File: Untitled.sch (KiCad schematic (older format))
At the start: 14 parts

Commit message: rest of the electrical
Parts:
- added D1, D2, D3, D4: D_Small, Diode_SMD:D_SOD-123, symbol Device:D_Small
- added F1: Polyfuse_Small, Fuse:Fuse_1206_3216Metric, symbol Device:Polyfuse_Small
- added MX1, MX2, MX3, MX4: MX-NoLED, MX_Alps_Hybrid:MX-1.5U-NoLED, symbol MX_Alps_Hybrid:MX-NoLED
- added USB1: Molex-0548190589, random-keyboard-parts:Molex-0548190589, symbol random-keyboard-parts:Molex-0548190589
- C1, C2, C3, C4, C5, C6, C7: renamed from C?; footprint (none) -> Capacitor_SMD:C_0805_2012Metric
- R1, R2, R3, R4: renamed from R?; footprint (none) -> Resistor_SMD:R_0805_2012Metric
- SW1: renamed from SW?; footprint (none) -> random-keyboard-parts:SKQG-1155865
- Y1: renamed from Y?; footprint (none) -> Crystal:Crystal_SMD_3225-4Pin_3.2x2.5mm
- gave numbers to parts that had none: 1
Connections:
- net +5V: now also F1.1
- net D+: now also USB1.4 (D-)
- net D-: now also USB1.3 (D+)
- net GND: now also USB1.1 (GND)
- new net: D1.2 (A), MX1.2 (ROW)
- new net: D4.2 (A), MX4.2 (ROW)
- new net: D2.2 (A), MX2.2 (ROW)
- new net: D3.2 (A), MX3.2 (ROW)
- new net COL0: MX1.1 (COL), MX2.1 (COL)
- new net COL1: MX3.1 (COL), MX4.1 (COL)
- new net ROW0: D1.1 (K), D4.1 (K)
- new net ROW1: D2.1 (K), D3.1 (K)
- new net VCC: F1.2, USB1.5 (VBUS)

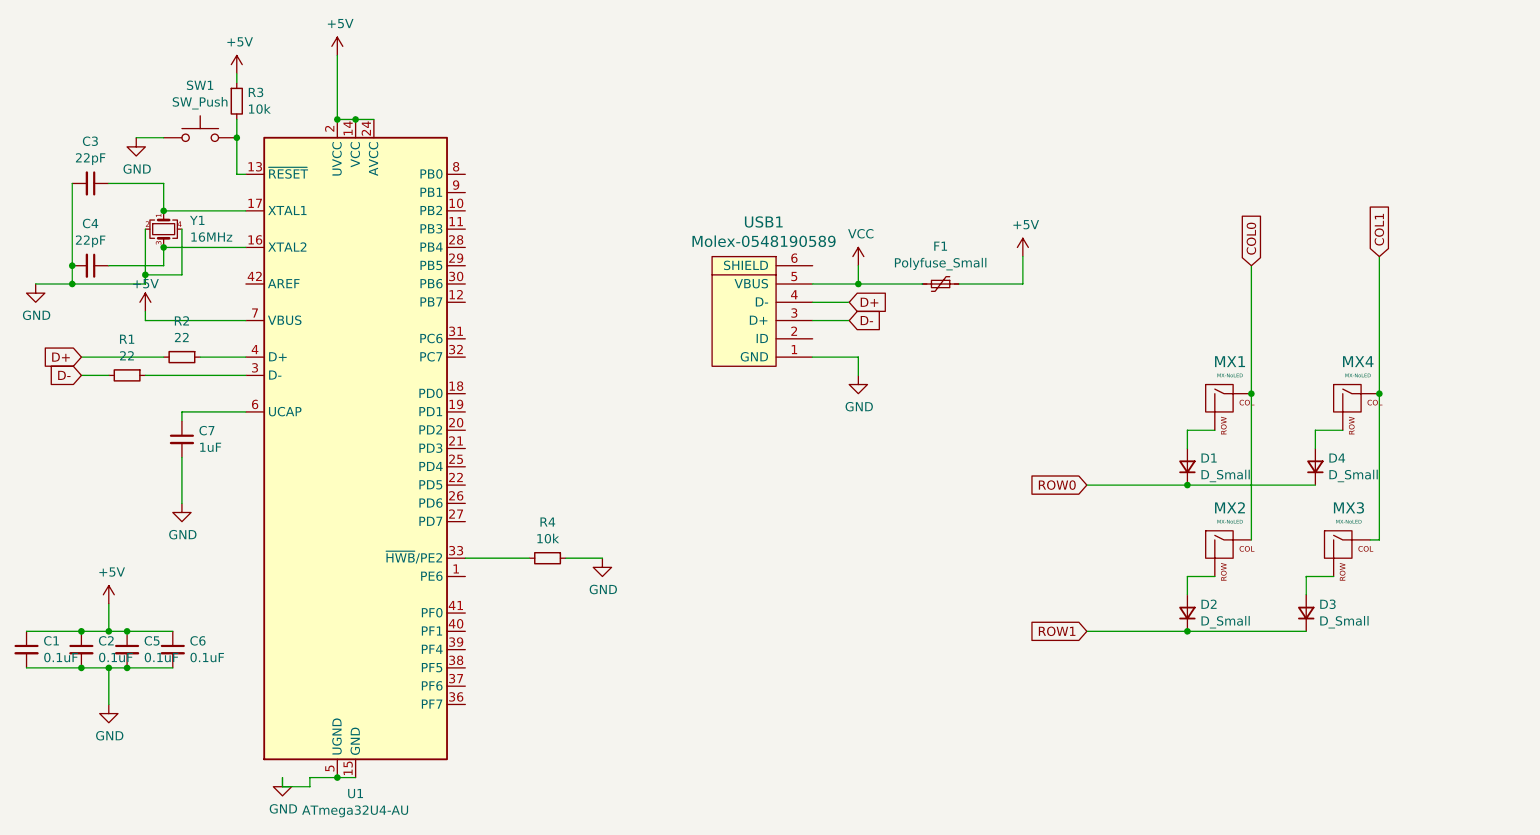
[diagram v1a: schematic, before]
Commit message: Routed MCU
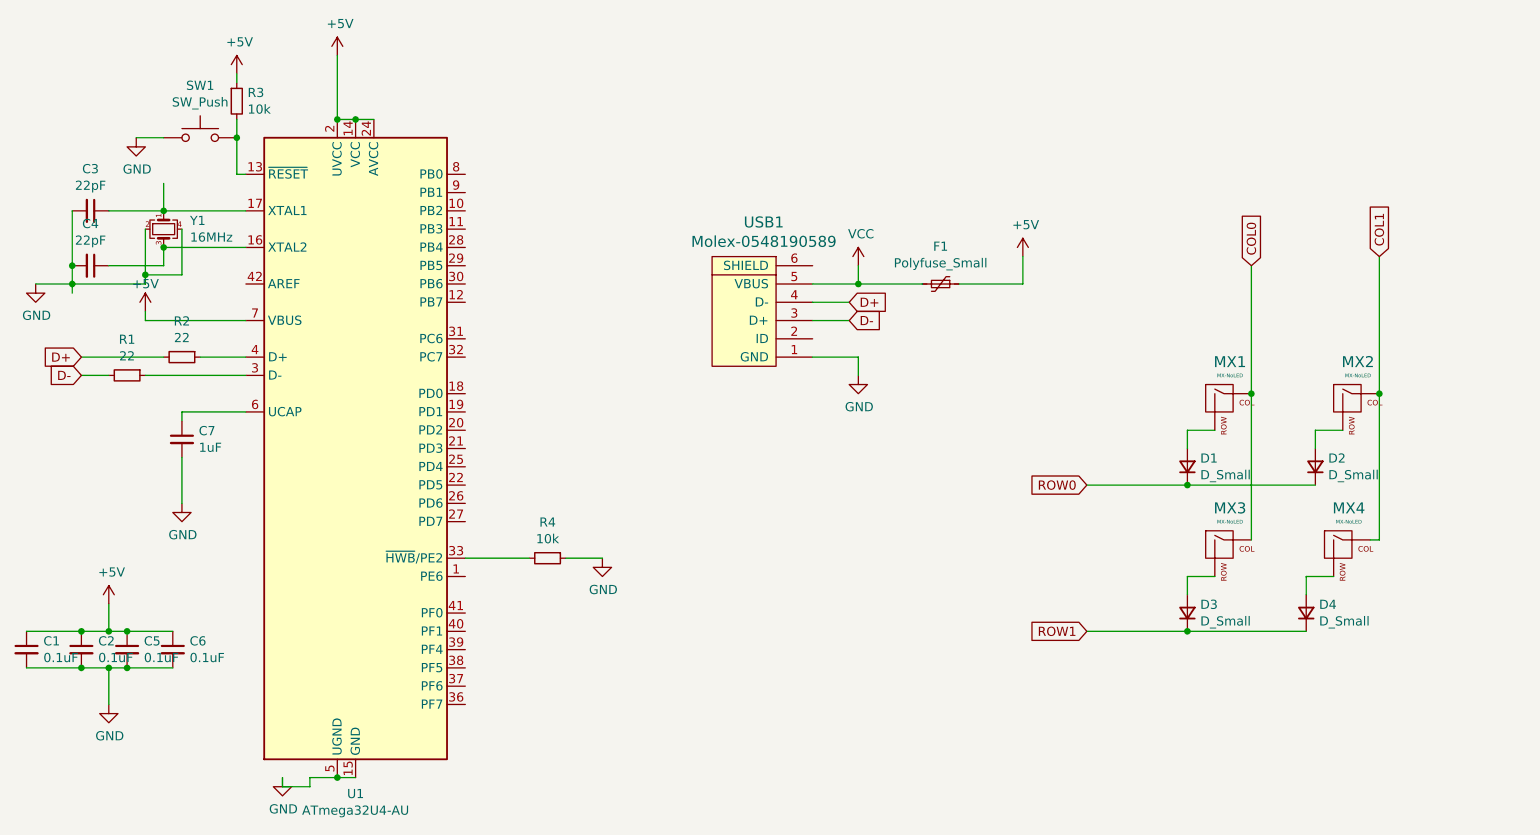
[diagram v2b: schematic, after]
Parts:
- renumbered D4 to D2, D2 to D3, D3 to D4, MX4 to MX2, MX2 to MX3, MX3 to MX4
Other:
- moved on the sheet: C3
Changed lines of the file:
@@
 L Device:C_Small C3
 U 1 1 60CC03DF
-P 1500 3300
-F 0 "C3" V 1271 3300 50  0000 C CNN
-F 1 "22pF" V 1362 3300 50  0000 C CNN
-F 2 "Capacitor_SMD:C_0805_2012Metric" H 1500 3300 50  0001 C CNN
-F 3 "~" H 1500 3300 50  0001 C CNN
-	1    1500 3300
+P 1500 3450
+F 0 "C3" V 1271 3450 50  0000 C CNN
+F 1 "22pF" V 1362 3450 50  0000 C CNN
+F 2 "Capacitor_SMD:C_0805_2012Metric" H 1500 3450 50  0001 C CNN
+F 3 "~" H 1500 3450 50  0001 C CNN
+	1    1500 3450
 	0    1    1    0
 $EndComp
@@
 	1900 3750 1900 3650
 Wire Wire Line
-	1600 3300 1900 3300
+	1600 3450 1900 3450
 Wire Wire Line
 	1900 3300 1900 3450
@@
 	1800 3850 1400 3850
 Wire Wire Line
-	1400 3300 1400 3750
+	1400 3450 1400 3750
 Wire Wire Line
 	1400 3750 1400 3850
@@
 	7500 4650 7500 4750
 $Comp
-L MX_Alps_Hybrid:MX-NoLED MX4
+L MX_Alps_Hybrid:MX-NoLED MX2
 U 1 1 60CF8F29
 P 8400 4500
-F 0 "MX4" H 8433 4723 60  0000 C CNN
+F 0 "MX2" H 8433 4723 60  0000 C CNN
 F 1 "MX-NoLED" H 8433 4649 20  0000 C CNN
 F 2 "MX_Alps_Hybrid:MX-1.5U-NoLED" H 7775 4475 60  0001 C CNN
@@
 $EndComp
 $Comp
-L Device:D_Small D4
+L Device:D_Small D2
 U 1 1 60CF8F2F
 P 8200 4850
-F 0 "D4" V 8246 4780 50  0000 R CNN
+F 0 "D2" V 8246 4780 50  0000 R CNN
 F 1 "D_Small" V 8155 4780 50  0000 R CNN
 F 2 "Diode_SMD:D_SOD-123" V 8200 4850 50  0001 C CNN
@@
 	8200 4650 8200 4750
 $Comp
-L MX_Alps_Hybrid:MX-NoLED MX2
+L MX_Alps_Hybrid:MX-NoLED MX3
 U 1 1 60CFABD6
 P 7700 5300
-F 0 "MX2" H 7733 5523 60  0000 C CNN
+F 0 "MX3" H 7733 5523 60  0000 C CNN
 F 1 "MX-NoLED" H 7733 5449 20  0000 C CNN
 F 2 "MX_Alps_Hybrid:MX-1.5U-NoLED" H 7075 5275 60  0001 C CNN
@@
 $EndComp
 $Comp
-L Device:D_Small D2
+L Device:D_Small D3
 U 1 1 60CFABDC
 P 7500 5650
-F 0 "D2" V 7546 5580 50  0000 R CNN
+F 0 "D3" V 7546 5580 50  0000 R CNN
 F 1 "D_Small" V 7455 5580 50  0000 R CNN
 F 2 "Diode_SMD:D_SOD-123" V 7500 5650 50  0001 C CNN
@@
 	7500 5450 7500 5550
 $Comp
-L MX_Alps_Hybrid:MX-NoLED MX3
+L MX_Alps_Hybrid:MX-NoLED MX4
 U 1 1 60CFC830
 P 8350 5300
-F 0 "MX3" H 8383 5523 60  0000 C CNN
+F 0 "MX4" H 8383 5523 60  0000 C CNN
 F 1 "MX-NoLED" H 8383 5449 20  0000 C CNN
 F 2 "MX_Alps_Hybrid:MX-1.5U-NoLED" H 7725 5275 60  0001 C CNN
@@
 $EndComp
 $Comp
-L Device:D_Small D3
+L Device:D_Small D4
 U 1 1 60CFC836
 P 8150 5650
-F 0 "D3" V 8196 5580 50  0000 R CNN
+F 0 "D4" V 8196 5580 50  0000 R CNN
 F 1 "D_Small" V 8105 5580 50  0000 R CNN
 F 2 "Diode_SMD:D_SOD-123" V 8150 5650 50  0001 C CNN
@@
 Wire Wire Line
 	8550 3700 8550 4450
+Wire Wire Line
+	1400 3850 1400 3900
 $EndSCHEMATC

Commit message: Keyboard  - ICSP  - Fixed USB D+/D-
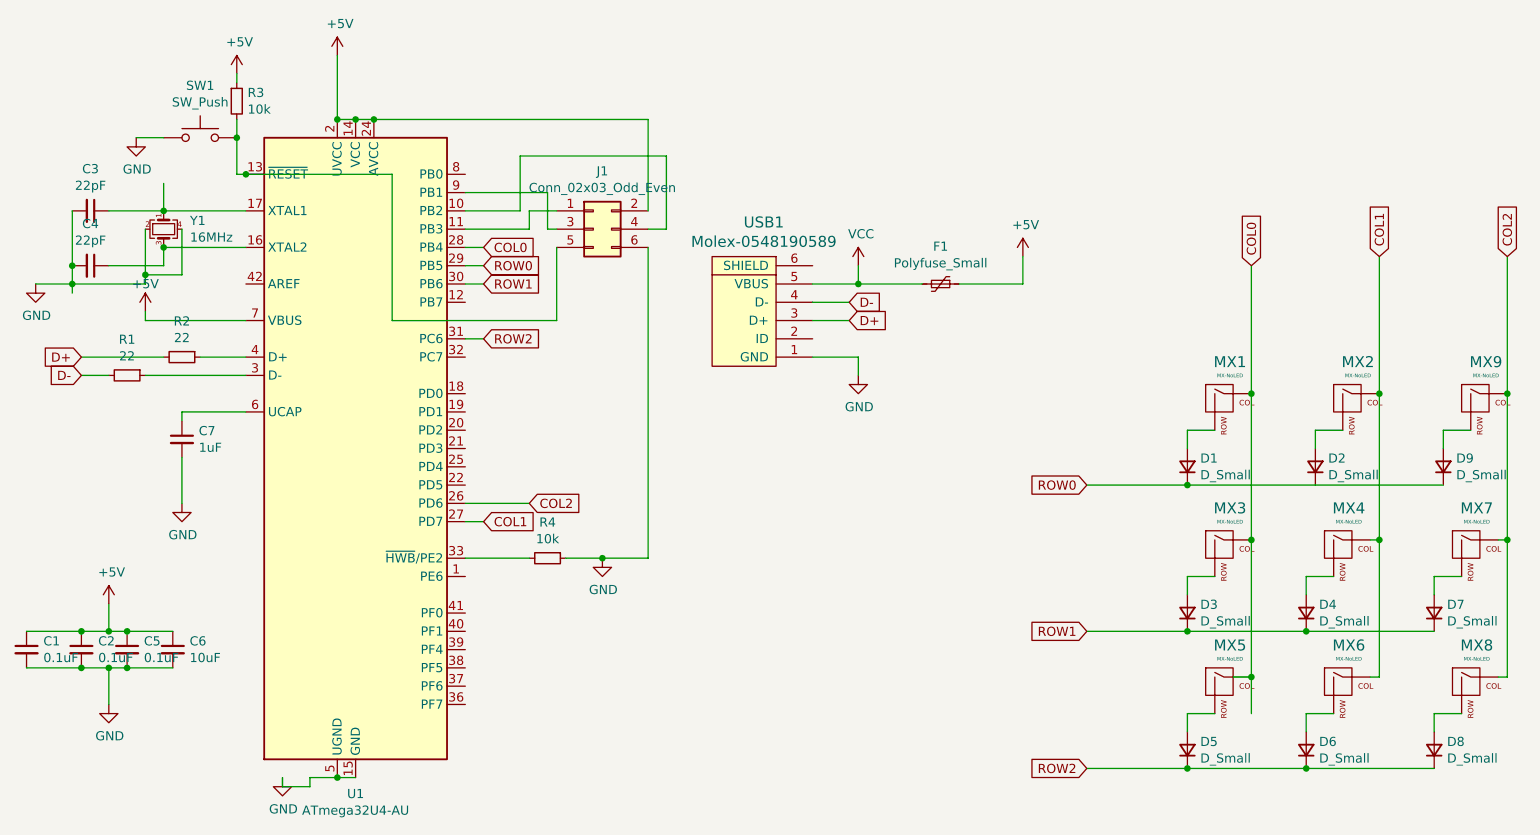
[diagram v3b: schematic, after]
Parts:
- added D5, D6, D7, D8, D9: D_Small, Diode_SMD:D_SOD-123, symbol Device:D_Small
- added J1: Conn_02x03_Odd_Even, Connector_PinHeader_2.54mm:PinHeader_2x03_P2.54mm_Vertical, symbol Connector_Generic:Conn_02x03_Odd_Even
- added MX5, MX6, MX7, MX8, MX9: MX-NoLED, MX_Alps_Hybrid:MX-1.5U-NoLED, symbol MX_Alps_Hybrid:MX-NoLED
- C6: value 0.1uF -> 10uF
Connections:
- net labels added: COL2, ROW2
- wire segments 75 -> 125
